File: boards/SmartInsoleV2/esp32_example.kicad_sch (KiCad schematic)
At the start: 54 parts, among them J1 Conn_01x02_Pin, J2 USB_B_Micro, J3 Conn_01x05_Female, J4 Conn_02x10_Odd_Even, J6 PJS008U-3000-0, J7 Conn_ARM_JTAG_SWD_10, Q2 SS8050-G, Q3 SS8050-G, SW1 SW_Push, SW2 SW_Push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

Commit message: Most of routing done
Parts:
- J6: footprint SmartInsolePCB:PJS008U30000 -> MEM2051-00-195-00-A:GCT_MEM2051-00-195-00-A
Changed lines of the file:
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@@
 			)
 		)
-		(property "Footprint" "SmartInsolePCB:PJS008U30000"
+		(property "Footprint" "MEM2051-00-195-00-A:GCT_MEM2051-00-195-00-A"
 			(at 260.35 315.9 0)
 			(effects

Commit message: added changes but not finished
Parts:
- removed H1, H2, H3, H4: MountingHole, MountingHole:MountingHole_3.2mm_M3, symbol Mechanical:MountingHole
- removed SW3, SW4: SW_Push, Button_Switch_SMD:SW_SPST_B3S-1000, symbol Switch:SW_Push
- added J5, J8: Conn_01x02_Pin, Connector_PinHeader_2.54mm:PinHeader_1x02_P2.54mm_Vertical, symbol Connector:Conn_01x02_Pin
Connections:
- net +3V3: now also J5.2 (Pin_2), J8.2 (Pin_2)
- net at R8.1: now also J8.1 (Pin_1)
- net at R6.1: now also J5.1 (Pin_1)
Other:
- title: ESP32 Example: Motor Controller -> Smart Insole

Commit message: re made board
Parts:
- C1, C2, C3, C4: footprint Capacitor_SMD:C_0603_1608Metric -> Capacitor_SMD:C_0805_2012Metric
- D3: footprint LED_SMD:LED_0603_1608Metric -> LED_SMD:LED_0805_2012Metric
- R1, R10, R11, R15, R16, R2, R3, R4, R5, R6, R7, R8: footprint Resistor_SMD:R_0603_1608Metric -> Resistor_SMD:R_0805_2012Metric
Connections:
- net PRESS1: now also U7.22 (IO14); no longer U7.11 (IO18)
- net PRESS10: now also U7.7 (IO7); no longer U7.24 (IO47)
- net PRESS2: now also U7.21 (IO13); no longer U7.12 (IO8)
- net PRESS3: now also U7.20 (IO12); no longer U7.17 (IO9)
- net PRESS4: now also U7.19 (IO11); no longer U7.18 (IO10)
- net PRESS5: now also U7.18 (IO10); no longer U7.19 (IO11)
- net PRESS6: now also U7.5 (IO5); no longer U7.20 (IO12)
- net PRESS7: now also U7.6 (IO6); no longer U7.21 (IO13)
- net PRESS8: now also U7.11 (IO18); no longer U7.22 (IO14)
- net PRESS9: now also U7.8 (IO15); no longer U7.23 (IO21)
- net SCL_6050: now also U7.17 (IO9); no longer U7.38 (IO2)
- net SDA_6050: now also U7.12 (IO8); no longer U7.39 (IO1)
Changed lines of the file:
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@@
 	(wire
 		(pts
-			(xy 358.14 68.58) (xy 361.95 68.58)
-		)
-		(stroke
-			(width 0)
-			(type default)
-		)
-	)
-	(wire
-		(pts
 			(xy 360.045 40.64) (xy 360.045 43.18)
 		)
@@
 	(wire
 		(pts
-			(xy 358.14 66.04) (xy 361.95 66.04)
-		)
-		(stroke
-			(width 0)
-			(type default)
-		)
-	)
-	(wire
-		(pts
 			(xy 283.21 53.34) (xy 283.21 54.61)
 		)
@@
 		)
 	)
-	(label "CHIP_PU"
-		(at 214.63 67.31 0)
+	(label "PRESS9"
+		(at 312.42 58.42 180)
 		(fields_autoplaced yes)
 		(effects
@@
 				(size 1.27 1.27)
 			)
-			(justify left bottom)
+			(justify right bottom)
 		)
 	)
-	(label "CS"
-		(at 237.49 220.98 180)
+	(label "PRESS6"
+		(at 312.42 50.8 180)
 		(fields_autoplaced yes)
 		(effects
@@
 		)
 	)
-	(label "SCL_6050"
-		(at 129.54 226.06 0)
+	(label "CHIP_PU"
+		(at 214.63 67.31 0)
 		(fields_autoplaced yes)
 		(effects
@@
 		)
 	)
-	(label "PRESS4"
-		(at 35.56 223.52 0)
+	(label "CS"
+		(at 237.49 220.98 180)
 		(fields_autoplaced yes)
 		(effects
@@
 				(size 1.27 1.27)
 			)
-			(justify left bottom)
+			(justify right bottom)
 		)
 	)
-	(label "PRESS9"
-		(at 312.42 96.52 180)
+	(label "SCL_6050"
+		(at 129.54 226.06 0)
 		(fields_autoplaced yes)
 		(effects
@@
 				(size 1.27 1.27)
 			)
-			(justify right bottom)
+			(justify left bottom)
 		)
 	)
-	(label "SDA_6050"
-		(at 361.95 66.04 0)
+	(label "PRESS4"
+		(at 35.56 223.52 0)
 		(fields_autoplaced yes)
 		(effects
@@
 		)
 	)
-	(label "PRESS5"
-		(at 312.42 86.36 180)
+	(label "PRESS8"
+		(at 312.42 66.04 180)
 		(fields_autoplaced yes)
 		(effects
@@
 		)
 	)
-	(label "PRESS10"
-		(at 312.42 99.06 180)
-		(fields_autoplaced yes)
-		(effects
-			(font
-				(size 1.27 1.27)
-			)
-			(justify right bottom)
-		)
-	)
 	(label "TX"
 		(at 21.59 156.21 180)
@@
 		)
 	)
-	(label "GPIO3_STRAPPING"
-		(at 312.42 76.2 180)
+	(label "PRESS3"
+		(at 312.42 88.9 180)
 		(fields_autoplaced yes)
 		(effects
@@
 		)
 	)
-	(label "GPIO46_STRAPPING"
-		(at 312.42 78.74 180)
+	(label "GPIO3_STRAPPING"
+		(at 312.42 76.2 180)
 		(fields_autoplaced yes)
 		(effects
@@
 		)
 	)
-	(label "PRESS6"
-		(at 312.42 88.9 180)
+	(label "GPIO46_STRAPPING"
+		(at 312.42 78.74 180)
 		(fields_autoplaced yes)
 		(effects
@@
 		)
 	)
+	(label "PRESS1"
+		(at 312.42 93.98 180)
+		(fields_autoplaced yes)
+		(effects
+			(font
+				(size 1.27 1.27)
+			)
+			(justify right bottom)
+		)
+	)
 	(label "D+"
 		(at 54.61 107.95 0)
@@
 		)
 	)
+	(label "PRESS7"
+		(at 312.42 53.34 180)
+		(fields_autoplaced yes)
+		(effects
+			(font
+				(size 1.27 1.27)
+			)
+			(justify right bottom)
+		)
+	)
 	(label "MTCK"
 		(at 361.95 83.82 0)
@@
 		)
 	)
-	(label "PRESS8"
-		(at 312.42 93.98 180)
+	(label "SCL_6050"
+		(at 312.42 81.28 180)
 		(fields_autoplaced yes)
 		(effects
@@
 		)
 	)
-	(label "PRESS1"
-		(at 312.42 66.04 180)
-		(fields_autoplaced yes)
-		(effects
-			(font
-				(size 1.27 1.27)
-			)
-			(justify right bottom)
-		)
-	)
 	(label "Start Hike"
 		(at 383.54 161.29 0)
@@
 		)
 	)
-	(label "PRESS7"
-		(at 312.42 91.44 180)
-		(fields_autoplaced yes)
-		(effects
-			(font
-				(size 1.27 1.27)
-			)
-			(justify right bottom)
-		)
-	)
 	(label "CS"
 		(at 361.95 93.98 0)
@@
 		)
 	)
+	(label "PRESS4"
+		(at 312.42 86.36 180)
+		(fields_autoplaced yes)
+		(effects
+			(font
+				(size 1.27 1.27)
+			)
+			(justify right bottom)
+		)
+	)
 	(label "SDA_6050"
 		(at 129.54 223.52 0)
@@
 		)
 	)
-	(label "SCL_6050"
-		(at 361.95 68.58 0)
+	(label "PRESS2"
+		(at 312.42 91.44 180)
 		(fields_autoplaced yes)
 		(effects
@@
 				(size 1.27 1.27)
 			)
-			(justify left bottom)
+			(justify right bottom)
 		)
 	)
@@
 		)
 	)
-	(label "PRESS2"
-		(at 312.42 68.58 180)
-		(fields_autoplaced yes)
-		(effects
-			(font
-				(size 1.27 1.27)
-			)
-			(justify right bottom)
-		)
-	)
 	(label "MOSI"
 		(at 361.95 88.9 0)
@@
 		)
 	)
-	(label "PRESS4"
-		(at 312.42 83.82 180)
-		(fields_autoplaced yes)
-		(effects
-			(font
-				(size 1.27 1.27)
-			)
-			(justify right bottom)
-		)
-	)
 	(label "MISO"
 		(at 361.95 91.44 0)
@@
 		)
 	)
+	(label "PRESS5"
+		(at 312.42 83.82 180)
+		(fields_autoplaced yes)
+		(effects
+			(font
+				(size 1.27 1.27)
+			)
+			(justify right bottom)
+		)
+	)
 	(label "End Hike"
 		(at 312.42 63.5 180)
@@
 		)
 	)
-	(label "PRESS3"
-		(at 312.42 81.28 180)
+	(label "PRESS10"
+		(at 312.42 55.88 180)
 		(fields_autoplaced yes)
 		(effects
@@
 		)
 	)
+	(label "SDA_6050"
+		(at 312.42 68.58 180)
+		(fields_autoplaced yes)
+		(effects
+			(font
+				(size 1.27 1.27)
+			)
+			(justify right bottom)
+		)
+	)
 	(label "GPIO0_STRAPPING"
 		(at 361.95 96.52 0)
@@
 			)
 		)
-		(property "Footprint" "Capacitor_SMD:C_0603_1608Metric"
+		(property "Footprint" "Capacitor_SMD:C_0805_2012Metric"
 			(at 278.13 140.97 0)
 			(effects
@@
 			)
 		)
-		(property "Footprint" "Resistor_SMD:R_0603_1608Metric"
+		(property "Footprint" "Resistor_SMD:R_0805_2012Metric"
 			(at 50.8 200.66 0)
 			(effects
@@
 			)
 		)
-		(property "Footprint" "Resistor_SMD:R_0603_1608Metric"
+		(property "Footprint" "Resistor_SMD:R_0805_2012Metric"
 			(at 50.8 261.62 0)
 			(effects
@@
 			)
 		)
-		(property "Footprint" "Capacitor_SMD:C_0603_1608Metric"
+		(property "Footprint" "Capacitor_SMD:C_0805_2012Metric"
 			(at 374.65 144.78 0)
 			(effects
@@
 			)
 		)
-		(property "Footprint" "Resistor_SMD:R_0603_1608Metric"
+		(property "Footprint" "Resistor_SMD:R_0805_2012Metric"
 			(at 50.8 269.24 0)
 			(effects
@@
 			)
 		)
-		(property "Footprint" "Resistor_SMD:R_0603_1608Metric"
+		(property "Footprint" "Resistor_SMD:R_0805_2012Metric"
 			(at 50.8 223.52 0)
 			(effects
@@
 			)
 		)
-		(property "Footprint" "Resistor_SMD:R_0603_1608Metric"
+		(property "Footprint" "Resistor_SMD:R_0805_2012Metric"
 			(at 50.8 231.14 0)
 			(effects
@@
 			)
 		)
-		(property "Footprint" "Resistor_SMD:R_0603_1608Metric"
+		(property "Footprint" "Resistor_SMD:R_0805_2012Metric"
 			(at 50.8 238.76 0)
 			(effects
@@
 			)
 		)
-		(property "Footprint" "Capacitor_SMD:C_0603_1608Metric"
+		(property "Footprint" "Capacitor_SMD:C_0805_2012Metric"
 			(at 374.65 165.1 0)
 			(effects
@@
 			)
 		)
-		(property "Footprint" "Resistor_SMD:R_0603_1608Metric"
+		(property "Footprint" "Resistor_SMD:R_0805_2012Metric"
 			(at 367.03 140.97 0)
 			(effects
@@
 			)
 		)
-		(property "Footprint" "Resistor_SMD:R_0603_1608Metric"
+		(property "Footprint" "Resistor_SMD:R_0805_2012Metric"
 			(at 50.8 208.28 0)
 			(effects
@@
 			)
 		)
-		(property "Footprint" "LED_SMD:LED_0603_1608Metric"
+		(property "Footprint" "LED_SMD:LED_0805_2012Metric"
 			(at 294.64 143.51 0)
 			(effects
@@
 			)
 		)
-		(property "Footprint" "Resistor_SMD:R_0603_1608Metric"
+		(property "Footprint" "Resistor_SMD:R_0805_2012Metric"
 			(at 50.8 246.38 0)
 			(effects
@@
 			)
 		)
-		(property "Footprint" "Resistor_SMD:R_0603_1608Metric"
+		(property "Footprint" "Resistor_SMD:R_0805_2012Metric"
 			(at 367.03 161.29 0)
 			(effects
@@
 			)
 		)
-		(property "Footprint" "Capacitor_SMD:C_0603_1608Metric"
+		(property "Footprint" "Capacitor_SMD:C_0805_2012Metric"
 			(at 228.6 140.97 0)
 			(effects
@@
 			)
 		)
-		(property "Footprint" "Resistor_SMD:R_0603_1608Metric"
+		(property "Footprint" "Resistor_SMD:R_0805_2012Metric"
 			(at 50.8 254 0)
 			(effects
@@
 			)
 		)
-		(property "Footprint" "Resistor_SMD:R_0603_1608Metric"
+		(property "Footprint" "Resistor_SMD:R_0805_2012Metric"
 			(at 50.8 215.9 0)
 			(effects

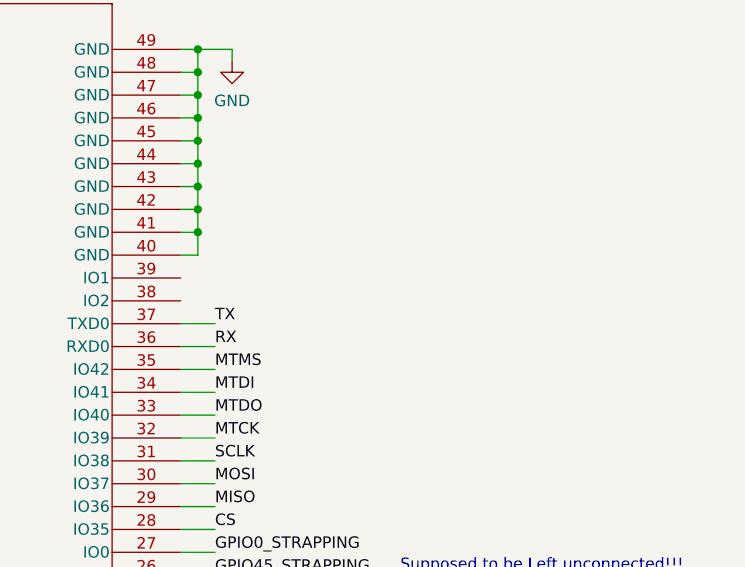
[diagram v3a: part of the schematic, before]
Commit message: 7 fine errors but need to double check the SD card footprint
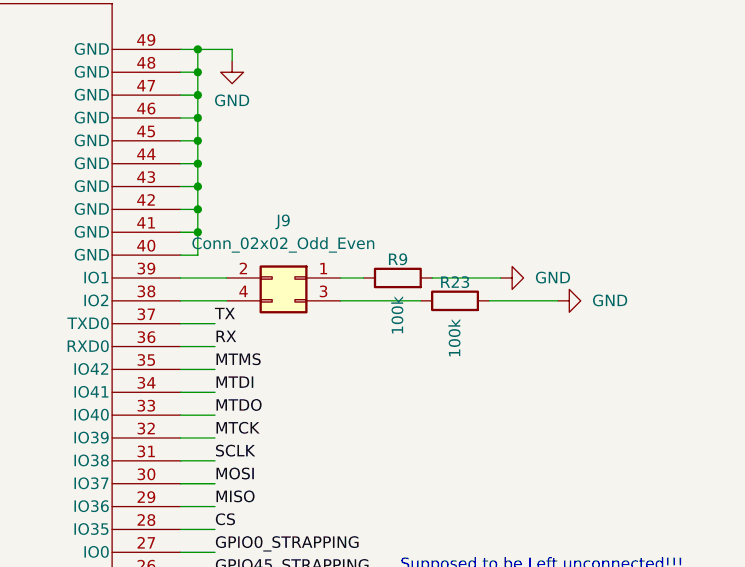
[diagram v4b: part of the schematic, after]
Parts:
- added J9: Conn_02x02_Odd_Even, Connector_PinHeader_2.54mm:PinHeader_2x02_P2.54mm_Vertical, symbol Connector_Generic:Conn_02x02_Odd_Even
- added R23, R9: 100k, Resistor_SMD:R_0805_2012Metric, symbol basic:R
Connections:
- net GND: now also R23.2, R9.2
- net at U7.38 (IO2): now also J9.4 (Pin_4)
- net at U7.39 (IO1): now also J9.2 (Pin_2)
- new net: J9.1 (Pin_1), R9.1
- new net: J9.3 (Pin_3), R23.1

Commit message: submitted for round 5
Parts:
- added C5: 1uF, Capacitor_SMD:C_0805_2012Metric, symbol Device:C_Small
- added J10: Conn_01x02_Pin, Connector_PinHeader_2.54mm:PinHeader_1x02_P2.54mm_Vertical, symbol Connector:Conn_01x02_Pin
- added R26: 5k, Resistor_SMD:R_0805_2012Metric, symbol Device:R_Small
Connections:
- net +3V3: now also J10.2 (Pin_2)
- net +5V: now also J1.1 (Pin_1)
- net GND: now also C5.2
- net POWER FROM BATTERY: no longer J1.1 (Pin_1)
- net Bluetooth: now reaches U7.24 (IO47)
- net Bluetooth: now also C5.1, R26.2
- new net: J10.1 (Pin_1), R26.1
